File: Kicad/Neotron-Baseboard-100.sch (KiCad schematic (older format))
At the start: 0 parts

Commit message: Imported top-level schematic from common.
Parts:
- added H101, H102, H103, H104, H105, H106, H107: MountingHole_Pad, MountingHole:MountingHole_4.3mm_M4_Pad_Via, symbol Mechanical:MountingHole_Pad
- added J101, J102, J103, J104: Neotron-Expansion-Slot, Neotron-Common-Hardware:Neotron-Expansion-Slot, symbol Neotron-Common-Hardware:Neotron-Expansion-Slot
- added LOGO101: OSHW Logo, Symbol:OSHW-Logo_11.4x12mm_SilkScreen, symbol Graphic:Logo_Open_Hardware_Small
- added LOGO102: Kicad Logo, Symbol:KiCad-Logo2_12mm_SilkScreen, symbol Graphic:Logo_Open_Hardware_Small
- added LOGO103: Neotron Logo, Neotron-Common-Hardware:logo, symbol Graphic:Logo_Open_Hardware_Small
- added U101: Neotron-CPU, Neotron-Common-Hardware:Neotron_CPU_Socket, symbol Neotron-Common-Hardware:Neotron-CPU
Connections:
- new net +3V3: J101.17 (3V3), J101.18 (3V3), J102.11 (EEPROM_ADDR0), J102.17 (3V3), J102.18 (3V3), J103.12 (EEPROM_ADDR1), J103.17 (3V3), J103.18 (3V3), J104.11 (EEPROM_ADDR0), J104.12 (EEPROM_ADDR1), J104.17 (3V3), J104.18 (3V3), U101.2.7 (3V3), U101.2.8 (3V3), U101.2.9 (3V3)
- new net +5V: J101.15 (5V), J101.16 (5V), J102.15 (5V), J102.16 (5V), J103.15 (5V), J103.16 (5V), J104.15 (5V), J104.16 (5V), U101.3.10 (5V), U101.3.11 (5V), U101.3.12 (5V)
- new net GND: H101.1, H102.1, H103.1, H104.1, H105.1, H106.1, H107.1, J101.11 (EEPROM_ADDR0), J101.12 (EEPROM_ADDR1), J101.13 (EEPROM_ADDR2), J101.19 (GND), J101.2 (GND), J101.20 (GND), J101.4 (GND), J101.6 (GND), J102.12 (EEPROM_ADDR1), J102.13 (EEPROM_ADDR2), J102.19 (GND), J102.2 (GND), J102.20 (GND), J102.4 (GND), J102.6 (GND), J103.11 (EEPROM_ADDR0), J103.13 (EEPROM_ADDR2), J103.19 (GND), J103.2 (GND), J103.20 (GND), J103.4 (GND), J103.6 (GND), J104.13 (EEPROM_ADDR2), J104.19 (GND), J104.2 (GND), J104.20 (GND), J104.4 (GND), J104.6 (GND), U101.2.10 (GND), U101.2.11 (GND), U101.2.12 (GND), U101.3.7 (GND), U101.3.8 (GND), U101.3.9 (GND)
- no-connect marks 0 -> 97
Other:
- note added: "All capacitors are 16V unless specified.\nAll resistors are 1% 1/4W unless specified."
- note added: "Common Sub-systems"
- note added: "Misc symbols"
- note added: "Slot 0"
- note added: "Slot 1"
- note added: "Slot 2"
- note added: "Slot 3"
- note added: "mini-ITX/micro-ATX\nMounting Holes"

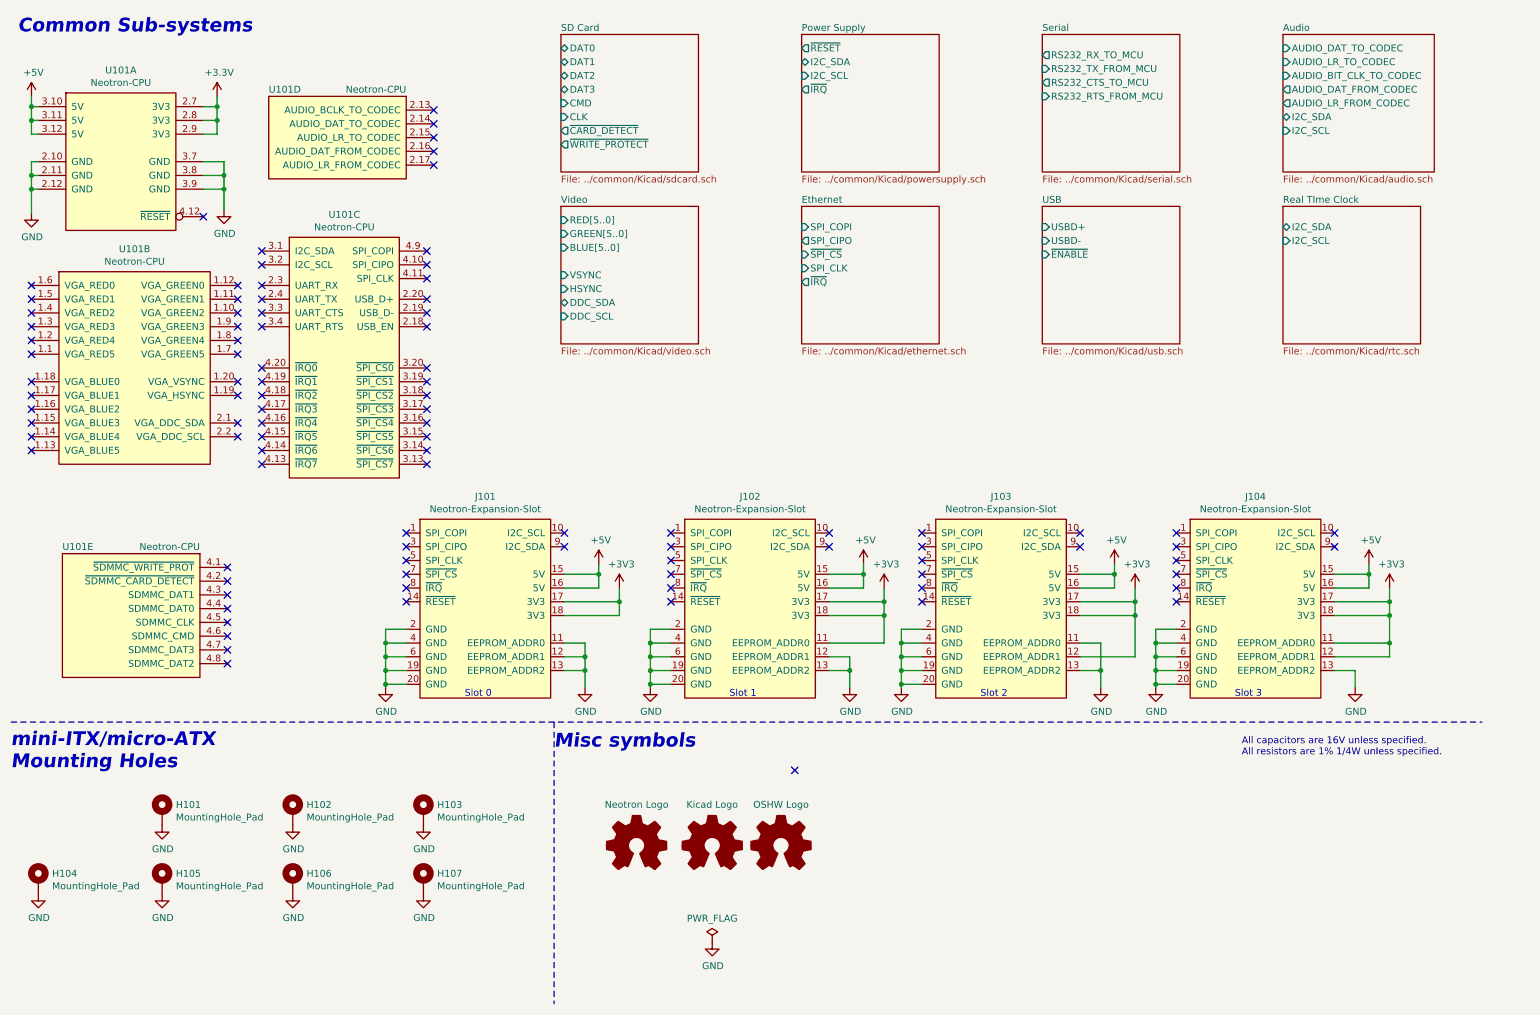
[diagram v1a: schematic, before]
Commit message: Wiring up top sheet.
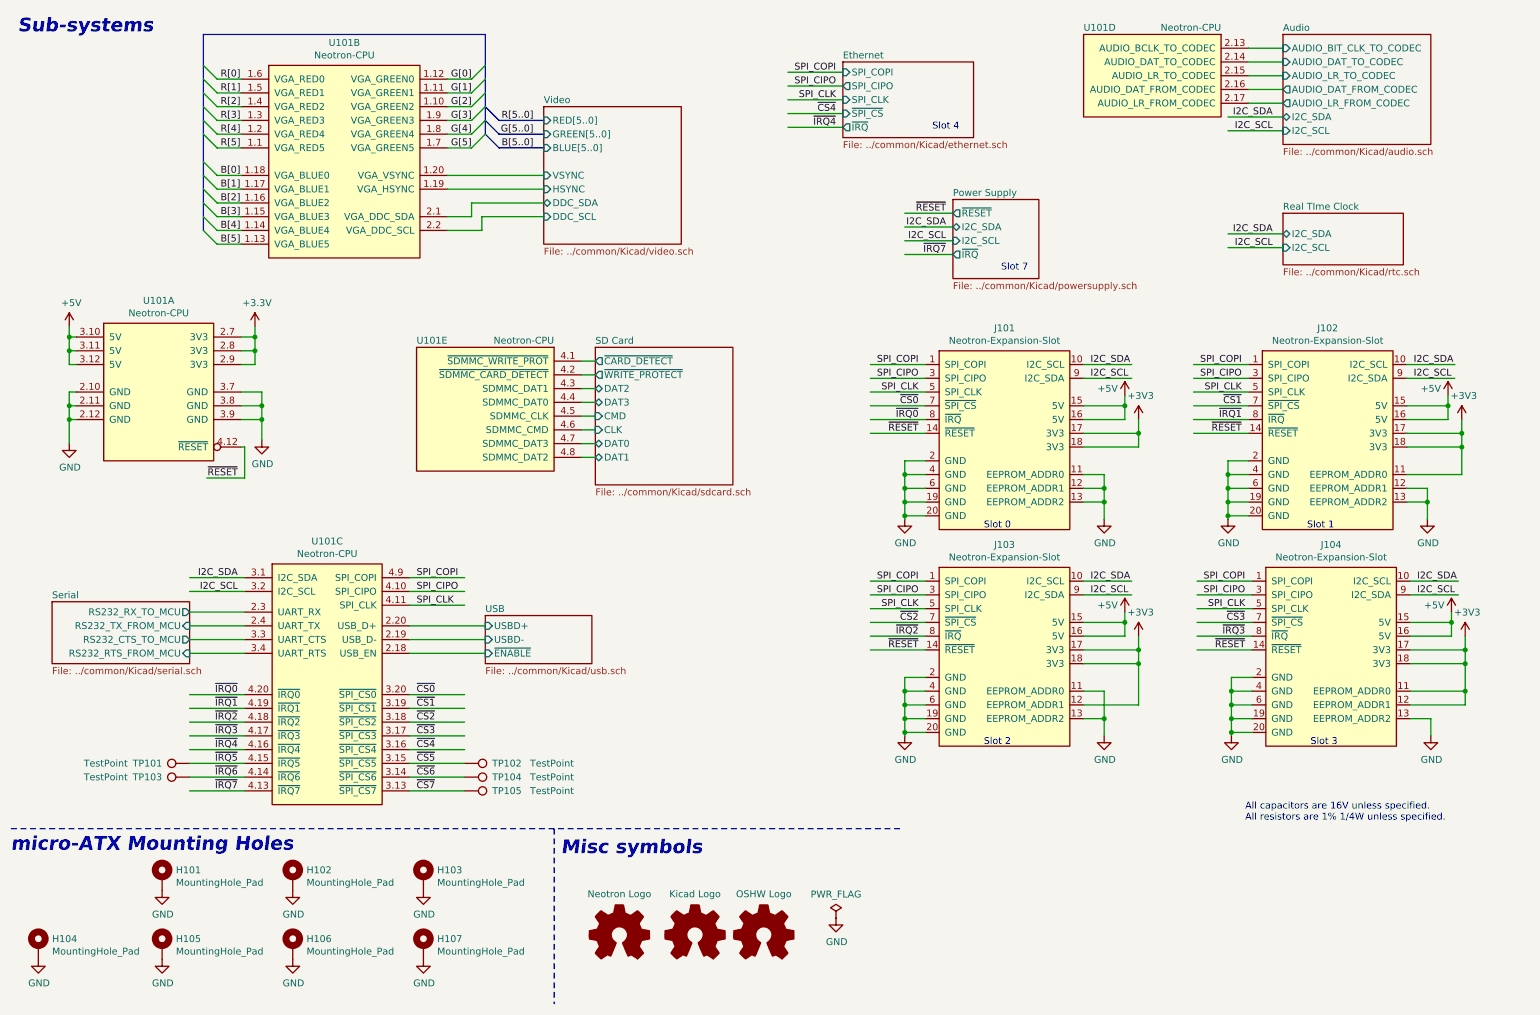
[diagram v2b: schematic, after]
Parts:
- added TP101, TP102, TP103, TP104, TP105: TestPoint, TestPoint:TestPoint_THTPad_D2.0mm_Drill1.0mm, symbol Connector:TestPoint
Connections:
- net labels added: B[0], B[1], B[2], B[3], B[4], B[5..0], B[5], G[0], G[1], G[2], G[3], G[4], G[5..0], G[5], I2C_SCL, I2C_SDA, R[0], R[1], R[2], R[3], R[4], R[5..0], R[5], SPI_CIPO, SPI_CLK, SPI_COPI, ~CS0, ~CS1, ~CS2, ~CS3, ~CS4, ~CS5, ~CS6, ~CS7, ~IRQ0, ~IRQ1, ~IRQ2, ~IRQ3, ~IRQ4, ~IRQ5, ~IRQ6, ~IRQ7, ~RESET
- wire segments 120 -> 235
- no-connect marks 97 -> 0
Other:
- note added: "Slot 4"
- note added: "Slot 7"
- note added: "Sub-systems"
- note added: "micro-ATX Mounting Holes"
- note removed: "Common Sub-systems"
- note removed: "mini-ITX/micro-ATX\nMounting Holes"
- moved on the sheet: H101, H102, H103, H104, H105, H106, H107, J101, J102, J103, J104, U101A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

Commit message: Updated common to 0.4.0 and added some part numbers.
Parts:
- H101, H102, H103, H104, H105, H106, H107: DNP 0 -> 1
- J101, J102, J103, J104: DNP (none) -> 0; Digikey (none) -> A31722-ND; MPN (none) -> 5-5530843-0; Manufacturer (none) -> TE
- TP101, TP102, TP103, TP104, TP105, U101: DNP (none) -> 1
- renumbered LOGO103 to LOGO101, LOGO101 to LOGO103
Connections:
- net labels added: B0, B1, B2, B3, B4, B5, B[0..5], G0, G1, G2, G3, G4, G5, G[0..5], R0, R1, R2, R3, R4, R5, R[0..5]
- net labels removed: B[0], B[1], B[2], B[3], B[4], B[5..0], B[5], G[0], G[1], G[2], G[3], G[4], G[5..0], G[5], R[0], R[1], R[2], R[3], R[4], R[5..0], R[5]

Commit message: Updating to common 0.5.0
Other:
- moved on the sheet: U101E
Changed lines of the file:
@@
 	1    0    0    -1
 $EndComp
-$Sheet
-S 4750 3025 1000 1000
-U 5FEF6B08
-F0 "SD Card" 50
-F1 "../common/Kicad/sdcard.sch" 50
-F2 "DAT2" B L 4750 3325 50
-F3 "DAT3" B L 4750 3425 50
-F4 "CMD" I L 4750 3525 50
-F5 "CLK" I L 4750 3625 50
-F6 "DAT0" B L 4750 3725 50
-F7 "DAT1" B L 4750 3825 50
-F8 "~CARD_DETECT" O L 4750 3125 50
-F9 "~WRITE_PROTECT" O L 4750 3225 50
-$EndSheet
 $Comp
 L power:PWR_FLAG #FLG0101
@@
 L Neotron-Common-Hardware:Neotron-CPU U101
 U 5 1 60173DE6
-P 3950 3325
-F 0 "U101" H 4450 3675 50  0000 R CNN
-F 1 "Neotron-CPU" H 3450 3675 50  0000 L CNN
-F 2 "Neotron-Common-Hardware:Neotron_CPU_Socket" H 4050 3875 50  0001 C CNN
-F 3 "https://github.com/neotron-compute" H 4850 3425 50  0001 C CNN
-F 4 "1" H 3950 3325 50  0001 C CNN "DNP"
-F 5 "~" H 3950 3325 50  0001 C CNN "Digikey"
-F 6 "~" H 3950 3325 50  0001 C CNN "MPN"
-F 7 "~" H 3950 3325 50  0001 C CNN "Manufacturer"
-	5    3950 3325
+P 4000 3400
+F 0 "U101" H 4500 3750 50  0000 R CNN
+F 1 "Neotron-CPU" H 3500 3750 50  0000 L CNN
+F 2 "Neotron-Common-Hardware:Neotron_CPU_Socket" H 4100 3950 50  0001 C CNN
+F 3 "https://github.com/neotron-compute" H 4900 3500 50  0001 C CNN
+F 4 "1" H 4000 3400 50  0001 C CNN "DNP"
+F 5 "~" H 4000 3400 50  0001 C CNN "Digikey"
+F 6 "~" H 4000 3400 50  0001 C CNN "MPN"
+F 7 "~" H 4000 3400 50  0001 C CNN "Manufacturer"
+	5    4000 3400
 	-1   0    0    -1
 $EndComp
@@
 F5 "~IRQ" O L 7350 2350 50
 $EndSheet
-Wire Wire Line
-	4650 3125 4750 3125
-Wire Wire Line
-	4750 3225 4650 3225
-Wire Wire Line
-	4650 3325 4750 3325
-Wire Wire Line
-	4750 3425 4650 3425
-Wire Wire Line
-	4650 3525 4750 3525
-Wire Wire Line
-	4750 3625 4650 3625
-Wire Wire Line
-	4650 3725 4750 3725
-Wire Wire Line
-	4750 3825 4650 3825
 Wire Wire Line
 	7350 2150 7000 2150
@@
 Text Label 2025 1075 0    50   ~ 0
 R0
+$Sheet
+S 4900 3100 710  905
+U 5FEF6B08
+F0 "SD Card" 50
+F1 "../common/Kicad/sdcard.sch" 50
+F2 "DAT2" B L 4900 3900 50
+F3 "DAT3" B L 4900 3800 50
+F4 "CMD" I L 4900 3700 50
+F5 "CLK" I L 4900 3600 50
+F6 "DAT0" B L 4900 3500 50
+F7 "DAT1" B L 4900 3400 50
+F8 "~CARD_DETECT" O L 4900 3200 50
+F9 "~WRITE_PROTECT" O L 4900 3300 50
+$EndSheet
+Wire Wire Line
+	4700 3200 4900 3200
+Wire Wire Line
+	4900 3300 4700 3300
+Wire Wire Line
+	4700 3400 4900 3400
+Wire Wire Line
+	4900 3500 4700 3500
+Wire Wire Line
+	4700 3600 4900 3600
+Wire Wire Line
+	4900 3700 4700 3700
+Wire Wire Line
+	4700 3800 4900 3800
+Wire Wire Line
+	4900 3900 4700 3900
 Wire Bus Line
 	3950 750  3950 1475

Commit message: Added I2C addresses.
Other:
- note added: "I2C Addressing\n* 0x1A : TLV320AIC23B Audio Codec\n* 0x50..0x57: ATC256 EEPROMs\n* 0x6F: MCP7940N RTC\n* 0x30: STM32F0 BMC\n"
- note added: "Slot 6"
- note removed: "Slot 4"
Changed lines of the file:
@@
 	7150 3650 6750 3650
 Text Notes 7200 1450 0    50   ~ 0
-Slot 4
+Slot 6
 Wire Wire Line
 	3400 4700 3800 4700
@@
 Wire Bus Line
 	1900 750  1900 2175
+Text Notes 9700 7050 0    50   ~ 0
+I2C Addressing\n* 0x1A : TLV320AIC23B Audio Codec\n* 0x50..0x57: ATC256 EEPROMs\n* 0x6F: MCP7940N RTC\n* 0x30: STM32F0 BMC\n
 $EndSCHEMATC
